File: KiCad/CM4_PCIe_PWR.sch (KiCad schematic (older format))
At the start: 0 parts

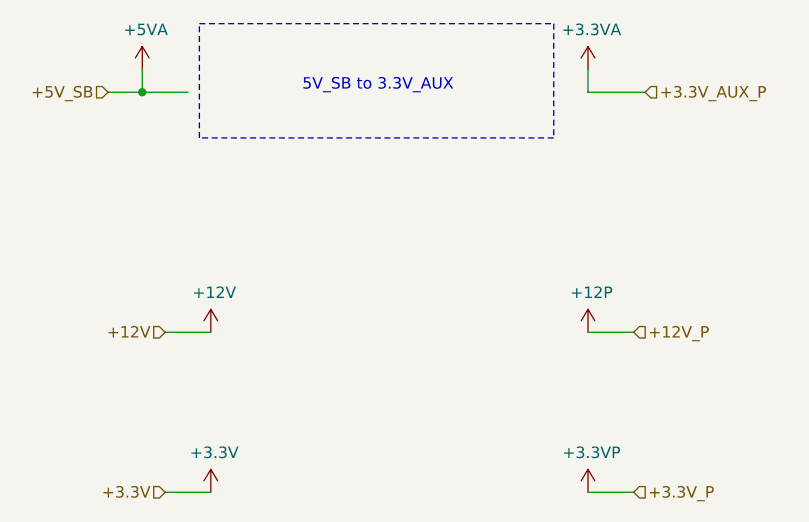
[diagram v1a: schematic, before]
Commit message: Added buffering caps to U2 (3.3vSB provider)
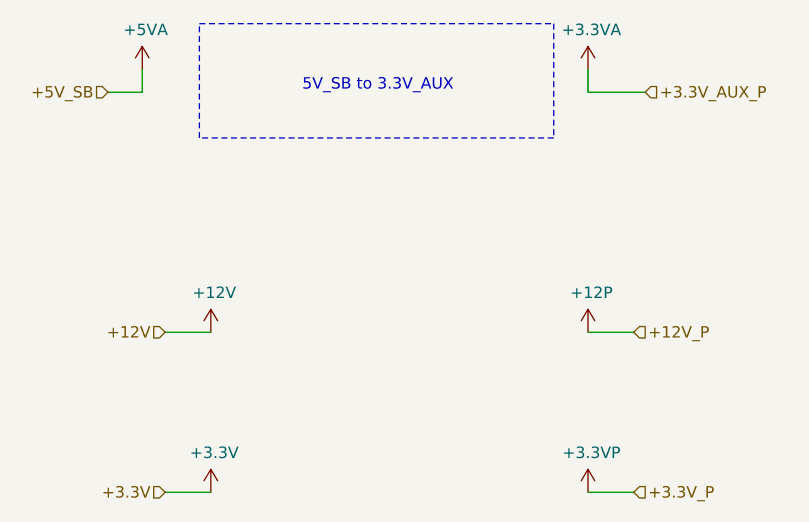
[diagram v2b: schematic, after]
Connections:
- wire segments 9 -> 8
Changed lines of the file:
@@
 $Descr A4 11693 8268
 encoding utf-8
-Sheet 11 16
+Sheet 5 16
 Title ""
 Date "2021-02-08"
@@
 Text HLabel 6750 2450 2    50   Input ~ 0
 +3.3V_AUX_P
-Wire Wire Line
-	4550 2450 4750 2450
 Text HLabel 4400 2450 0    50   Input ~ 0
 +5V_SB
@@
 Wire Wire Line
 	4550 2450 4550 2350
-Connection ~ 4550 2450
 Wire Wire Line
 	6500 2350 6500 2450
